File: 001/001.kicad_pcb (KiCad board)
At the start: 2 copper layers, 75 x 98.8 mm, 55 parts

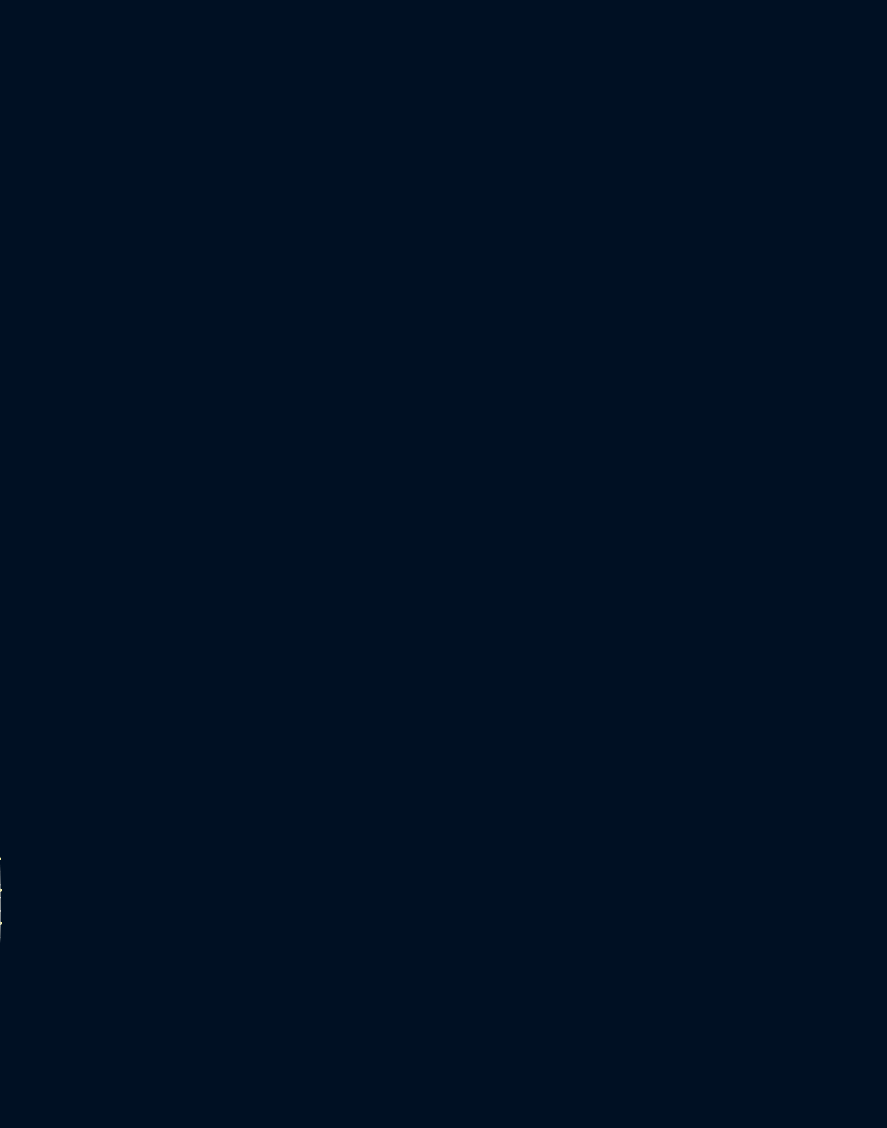
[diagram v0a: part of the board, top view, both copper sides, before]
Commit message: Add new shapes
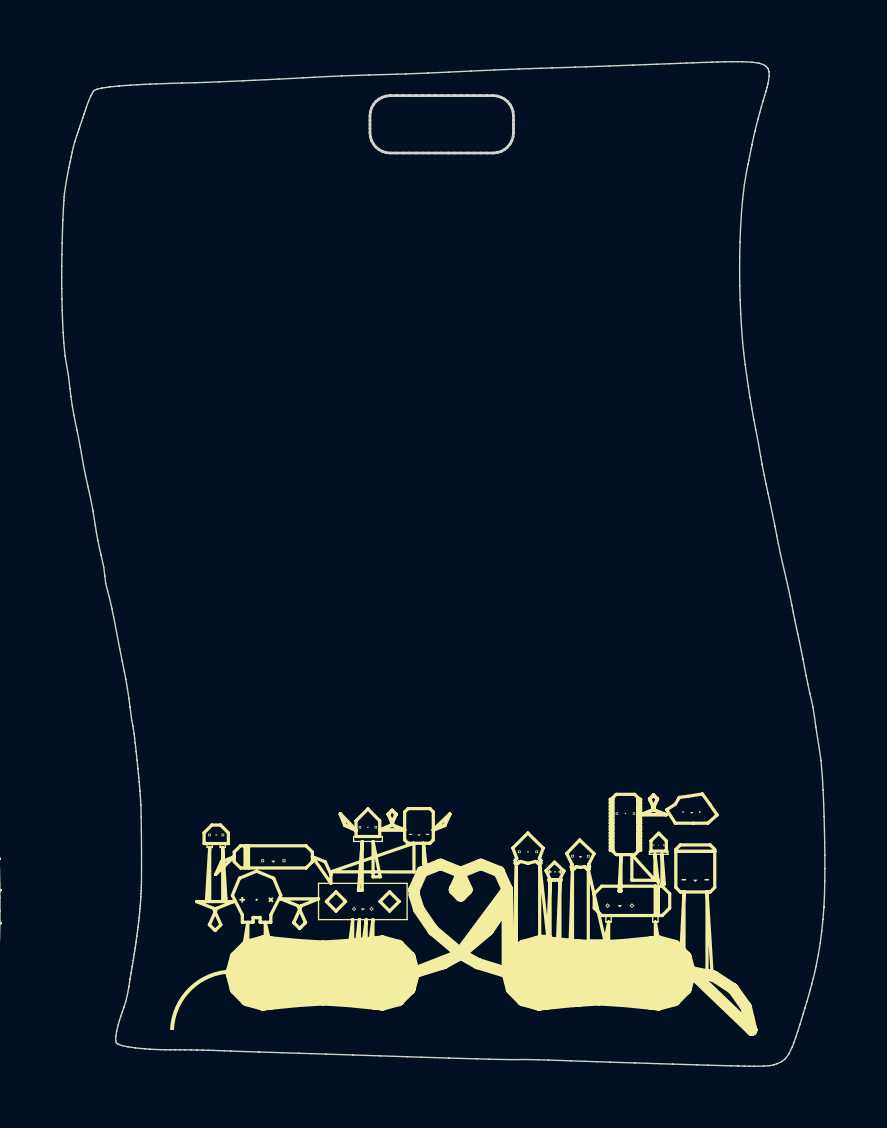
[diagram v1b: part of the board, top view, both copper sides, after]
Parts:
- added svg2mod: G***, ArduinoBadge:2019.01, F.Cu at (214.4, 106.6)
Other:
- outline, holes or cut-outs redrawn
